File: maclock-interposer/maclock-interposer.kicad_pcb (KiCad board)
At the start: 2 copper layers, 52.1 x 25.9 mm, 3 parts, among them J1 HC-PM254-8.5H-2x20PS, J2 PZ254V-11-07P, J3 HB-PH9-254220PB2GOP

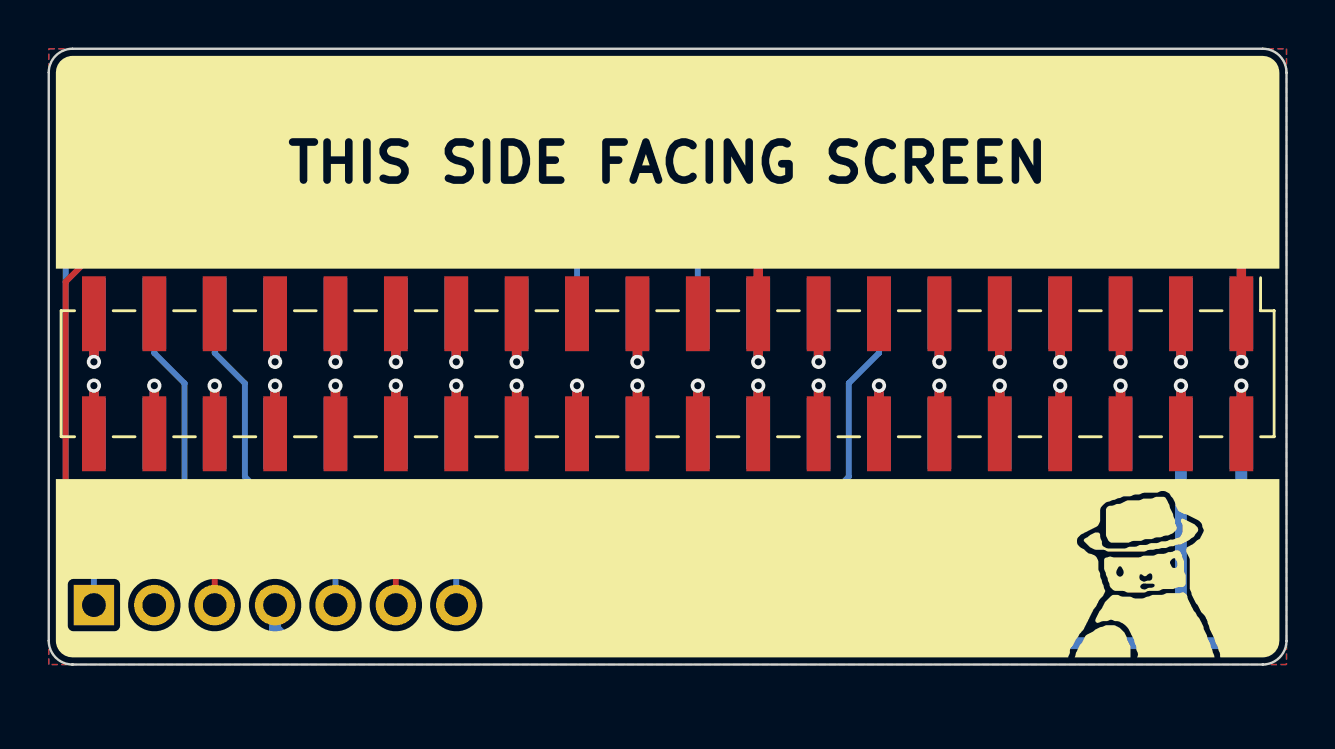
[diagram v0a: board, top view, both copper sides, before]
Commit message: Interposer J2: female socket on the screen side, 1.5 mm further south
The cable now plugs in from the screen side, so J2 is a 1x7 female
socket (XFCN PM254V-11-07-H85, LCSC C2832270) on top, in the same pin
order. The board grows 1.5 mm south to make room, and J2's labels move
to both sides and read "Dial A" / "Dial B" like the breakout's. ENC_A
and BTN2 are re-routed so the screen-side lettering sits on unbroken
silk. Schematic fields carry manufacturer, MPN and LCSC for all three
connectors.
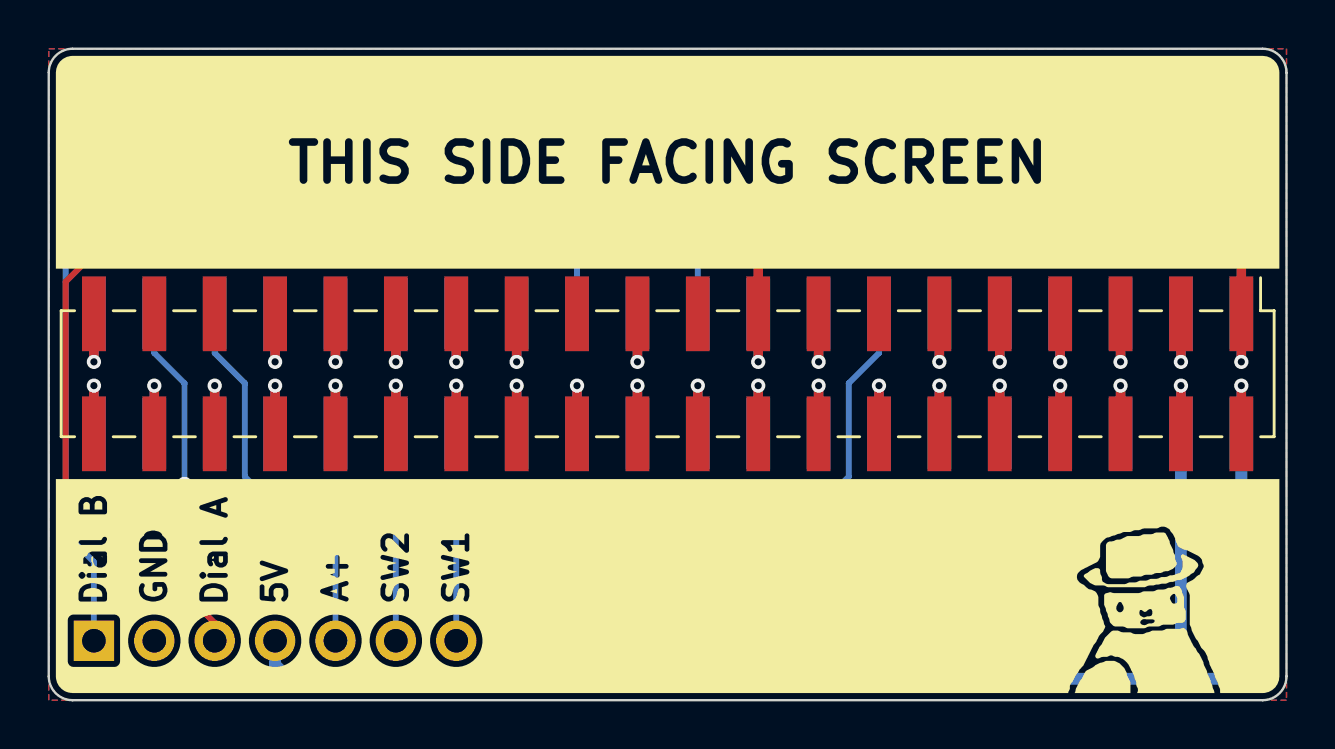
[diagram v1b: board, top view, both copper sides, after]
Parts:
- J2: value PZ254V-11-07P -> PM254V-11-07-H85; footprint Connector_PinHeader_2.54mm:PinHeader_1x07_P2.54mm_Vertical -> Connector_PinSocket_2.54mm:PinSocket_1x07_P2.54mm_Vertical; moved to F.Cu
- moved J2 1.50 mm to (101.7, 112.5), turned to 90 degrees
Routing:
- net /5V: track 61.0 -> 64.0 mm
- net /ENC_A: track 42.1 -> 43.8 mm
- net /AUDIO: track 15.1 -> 16.6 mm
- net /ENC_B: track 43.8 -> 45.3 mm
- net /BTN2: track 20.4 -> 21.9 mm, vias 1 -> 2
- net /BTN1: track 27.8 -> 29.3 mm
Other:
- board size 52.1 x 25.9 mm -> 52.1 x 27.4 mm
- board text added: "Dial A"
- board text added: "Dial B"
- board text added: "rev 2026.10"
- board text removed: "A"
- board text removed: "B"
- board text removed: "rev 2026.09"

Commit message: Interposer: rev 2026.11 on the silkscreen
It ships in the same order as the breakout's rev 2026.11, so it carries the
same rev. Silkscreen text only; the README's back render still shows
2026.10.
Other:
- board text added: "rev 2026.11"
- board text removed: "rev 2026.10"
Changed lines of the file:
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@@
 		)
 	)
-	(gr_text "rev 2026.10"
+	(gr_text "rev 2026.11"
 		(at 114.5 95.25 0)
 		(layer "B.SilkS")

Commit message: Interposer: source location and licence on the Pi-side silkscreen
The interposer's LICENSE asks, per section 4 of the CERN-OHL-S v2, for the
source location on the board's silkscreen where practicable. The same line
as on the breakout, "github.com/wr/macintosh-mini   CERN-OHL-S-2.0", now
runs in 0.8 mm text (0.15 stroke) on B.SilkS, in the free band between the
header and the "by Wells Workshop" by-line, centred at (134.9, 106.9). It
is the only free run on the Pi side that takes it in one line. On the
screen side it would have to be knocked out of the silk fill, and 0.8 mm
knock-outs fill in.

Clearance: at least 0.69 mm to the board edge, 0.73 mm to the SW1 label,
0.88 mm to J1's pads, and more to the vias.

Pi-side render refreshed with the same recipe as dfea1f2/a710e63 (which
reproduces the committed image from the previous board to within
quantisation noise). The screen-side render is unchanged.

DRC as before (J2 lib_footprint_mismatch, Garamond text-thickness
warning), 0 unconnected, schematic parity clean, with and without
--refill-zones.
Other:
- board text added: "github.com/wr/macintosh-mini CERN-OHL-S-2.0"
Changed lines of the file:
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@@
 		(layer "Edge.Cuts")
+	)
+	(gr_text "github.com/wr/macintosh-mini   CERN-OHL-S-2.0"
+		(at 134.9 106.9 0)
+		(layer "B.SilkS")
+		(effects
+			(font
+				(size 0.8 0.8)
+				(thickness 0.15)
+			)
+			(justify mirror)
+		)
 	)
 	(gr_text "Dial B"
